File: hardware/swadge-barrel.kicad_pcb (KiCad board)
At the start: 2 copper layers, 70.4 x 89.6 mm, 45 parts, among them J1 USB_B_Micro, Q1 Q_NPN_BEC, SW4 SW_SPDT, U1 ESP-13-WROOM-02D, U2 DISP_OLED_UG-2864HSWEG01, U3 BUS_PCIexpress, U4 QMA6981, U5 AP1117-33

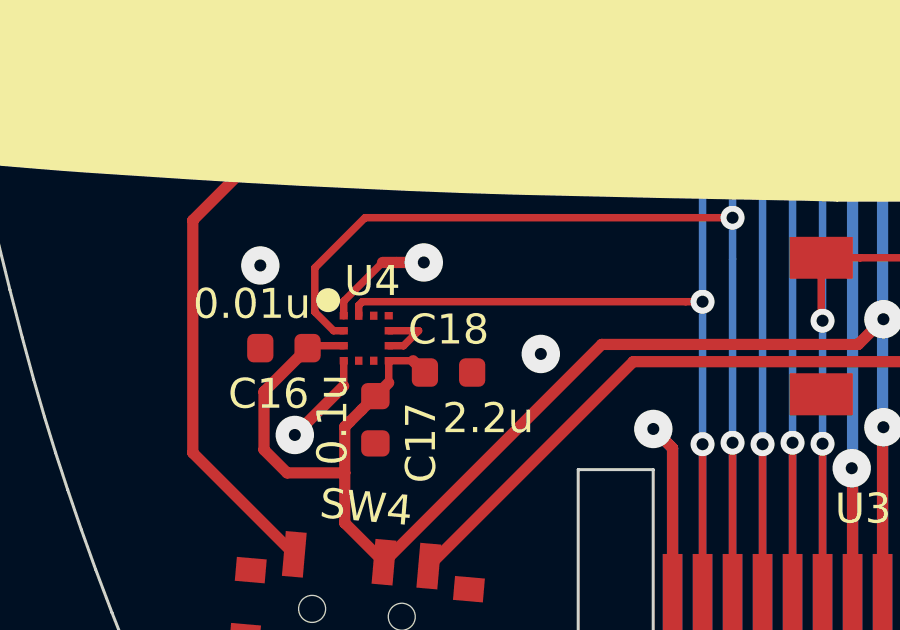
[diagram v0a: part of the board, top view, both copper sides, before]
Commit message: Updated ESP model
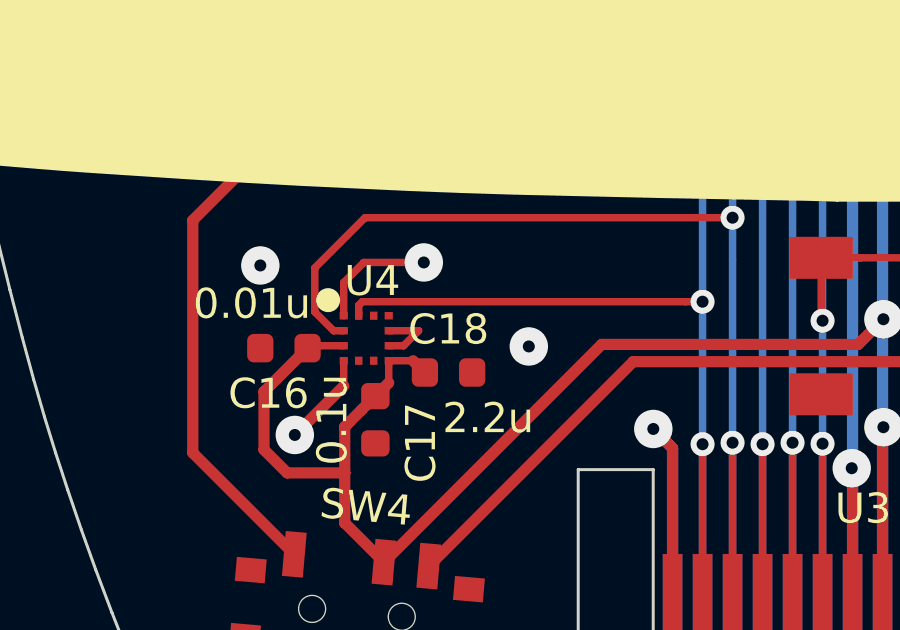
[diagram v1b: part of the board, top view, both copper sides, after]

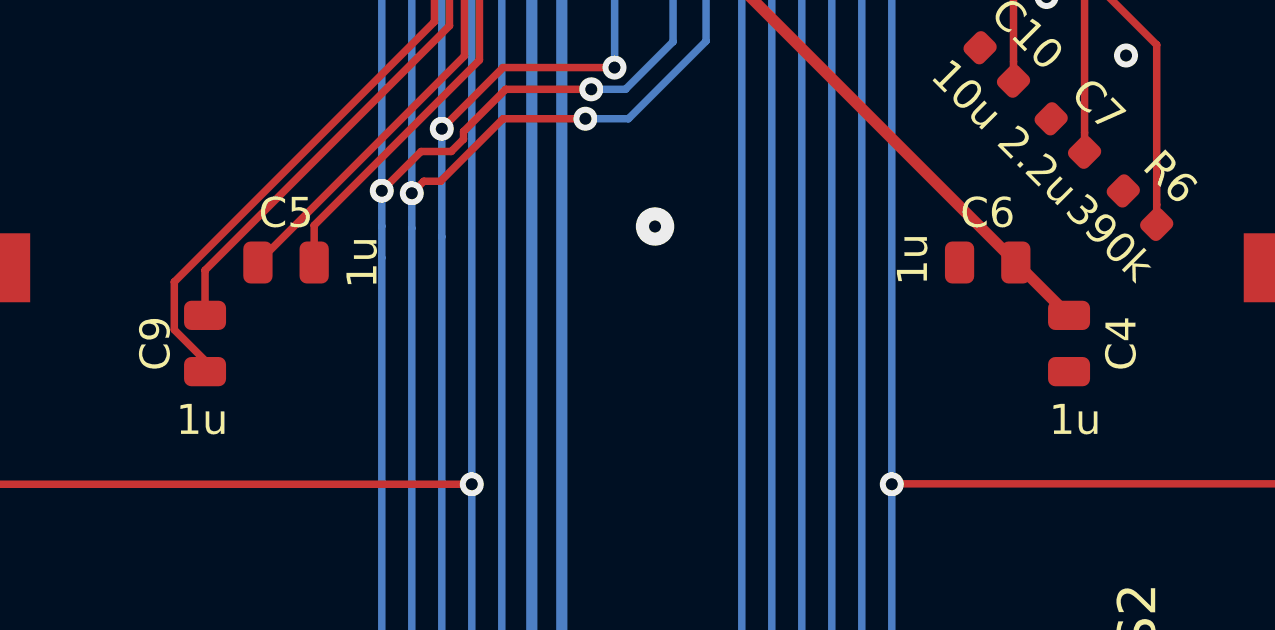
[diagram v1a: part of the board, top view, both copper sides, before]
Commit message: Added 0ohm support resistors
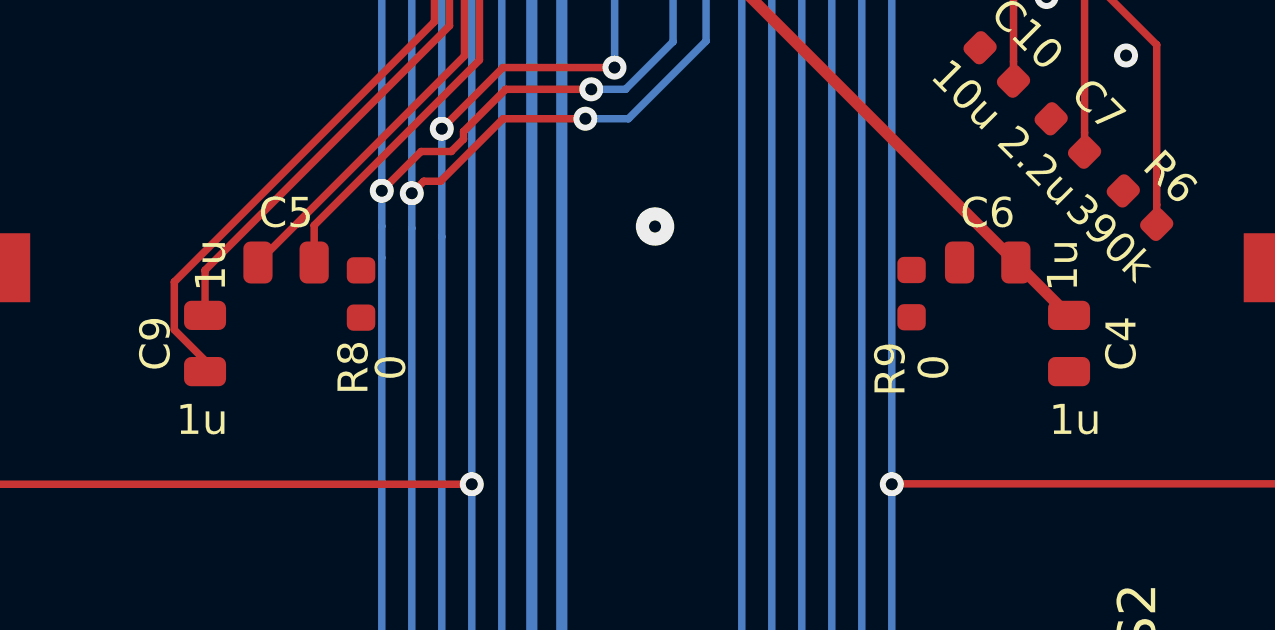
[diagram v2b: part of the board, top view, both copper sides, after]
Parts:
- added R8: 0, Swadge_Parts:R_0603_1608Metric, F.Cu at (136.3, 94.8)
- added R9: 0, Swadge_Parts:R_0603_1608Metric, F.Cu at (154.7, 94.8)
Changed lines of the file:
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@@
     (tracks 493)
     (zones 0)
-    (modules 45)
+    (modules 47)
     (nets 41)
   )
@@
     (uvia_drill 0.1)
   )
+  (module Swadge_Parts:R_0603_1608Metric (layer F.Cu)
+    (at 154.65 94.8375 90)
+    (descr "Resistor SMD 0603 (1608 Metric), square (rectangular) end terminal, IPC_7351 nominal, (Body size source: http://www.tortai-tech.com/upload/download/2011102023233369053.pdf), generated with kicad-footprint-generator")
+    (tags resistor)
+    (attr smd)
+    (fp_text reference R9 (at -2.5125 -0.7 90) (layer F.SilkS)
+      (effects (font (size 1 1) (thickness 0.15)))
+    )
+    (fp_text value 0 (at -2.4625 0.75 90) (layer F.SilkS)
+      (effects (font (size 1 1) (thickness 0.15)))
+    )
+    (fp_line (start -0.8 0.4) (end -0.8 -0.4) (layer F.Fab) (width 0.1))
+    (fp_line (start -0.8 -0.4) (end 0.8 -0.4) (layer F.Fab) (width 0.1))
+    (fp_line (start 0.8 -0.4) (end 0.8 0.4) (layer F.Fab) (width 0.1))
+    (fp_line (start 0.8 0.4) (end -0.8 0.4) (layer F.Fab) (width 0.1))
+    (fp_line (start -0.162779 -0.51) (end 0.162779 -0.51) (layer F.Fab) (width 0.12))
+    (fp_line (start -0.162779 0.51) (end 0.162779 0.51) (layer F.Fab) (width 0.12))
+    (fp_line (start -1.48 0.73) (end -1.48 -0.73) (layer F.CrtYd) (width 0.05))
+    (fp_line (start -1.48 -0.73) (end 1.48 -0.73) (layer F.CrtYd) (width 0.05))
+    (fp_line (start 1.48 -0.73) (end 1.48 0.73) (layer F.CrtYd) (width 0.05))
+    (fp_line (start 1.48 0.73) (end -1.48 0.73) (layer F.CrtYd) (width 0.05))
+    (fp_text user %R (at 0 0 90) (layer F.Fab)
+      (effects (font (size 0.4 0.4) (thickness 0.06)))
+    )
+    (pad 1 smd roundrect (at -0.7875 0 90) (size 0.875 0.95) (layers F.Cu F.Paste F.Mask) (roundrect_rratio 0.25)
+      (net 1 GND))
+    (pad 2 smd roundrect (at 0.7875 0 90) (size 0.875 0.95) (layers F.Cu F.Paste F.Mask) (roundrect_rratio 0.25)
+      (net 1 GND))
+    (model ${KIPRJMOD}/kicad-libs/package3d/R_0603_1608Metric.wrl
+      (at (xyz 0 0 0))
+      (scale (xyz 1 1 1))
+      (rotate (xyz 0 0 0))
+    )
+  )
+  (module Swadge_Parts:R_0603_1608Metric (layer F.Cu)
+    (at 136.3 94.85 90)
+    (descr "Resistor SMD 0603 (1608 Metric), square (rectangular) end terminal, IPC_7351 nominal, (Body size source: http://www.tortai-tech.com/upload/download/2011102023233369053.pdf), generated with kicad-footprint-generator")
+    (tags resistor)
+    (attr smd)
+    (fp_text reference R8 (at -2.45 -0.25 90) (layer F.SilkS)
+      (effects (font (size 1 1) (thickness 0.15)))
+    )
+    (fp_text value 0 (at -2.45 1 90) (layer F.SilkS)
+      (effects (font (size 1 1) (thickness 0.15)))
+    )
+    (fp_line (start -0.8 0.4) (end -0.8 -0.4) (layer F.Fab) (width 0.1))
+    (fp_line (start -0.8 -0.4) (end 0.8 -0.4) (layer F.Fab) (width 0.1))
+    (fp_line (start 0.8 -0.4) (end 0.8 0.4) (layer F.Fab) (width 0.1))
+    (fp_line (start 0.8 0.4) (end -0.8 0.4) (layer F.Fab) (width 0.1))
+    (fp_line (start -0.162779 -0.51) (end 0.162779 -0.51) (layer F.Fab) (width 0.12))
+    (fp_line (start -0.162779 0.51) (end 0.162779 0.51) (layer F.Fab) (width 0.12))
+    (fp_line (start -1.48 0.73) (end -1.48 -0.73) (layer F.CrtYd) (width 0.05))
+    (fp_line (start -1.48 -0.73) (end 1.48 -0.73) (layer F.CrtYd) (width 0.05))
+    (fp_line (start 1.48 -0.73) (end 1.48 0.73) (layer F.CrtYd) (width 0.05))
+    (fp_line (start 1.48 0.73) (end -1.48 0.73) (layer F.CrtYd) (width 0.05))
+    (fp_text user %R (at 0 0 90) (layer F.Fab)
+      (effects (font (size 0.4 0.4) (thickness 0.06)))
+    )
+    (pad 1 smd roundrect (at -0.7875 0 90) (size 0.875 0.95) (layers F.Cu F.Paste F.Mask) (roundrect_rratio 0.25)
+      (net 1 GND))
+    (pad 2 smd roundrect (at 0.7875 0 90) (size 0.875 0.95) (layers F.Cu F.Paste F.Mask) (roundrect_rratio 0.25)
+      (net 1 GND))
+    (model ${KIPRJMOD}/kicad-libs/package3d/R_0603_1608Metric.wrl
+      (at (xyz 0 0 0))
+      (scale (xyz 1 1 1))
+      (rotate (xyz 0 0 0))
+    )
+  )
   (module Swadge_Parts:ESP-13-WROOM-02 (layer F.Cu)
     (at 148.509589 60.463179 357)
@@
       (effects (font (size 1 1) (thickness 0.15)))
     )
-    (fp_text value 1u (at -2.4879 -0.1 90) (layer F.SilkS)
+    (fp_text value 1u (at 2.5121 0.1 90) (layer F.SilkS)
       (effects (font (size 1 1) (thickness 0.15)))
     )
@@
       (effects (font (size 1 1) (thickness 0.15)))
     )
-    (fp_text value 1u (at 2.55 0 90) (layer F.SilkS)
-      (effects (font (size 1 1) (thickness 0.15)))
-    )
+    (fp_text value 1u (at -2.5 0.1 90) (layer F.SilkS)
+      (effects (font (size 1 1) (thickness 0.15)))
+    )

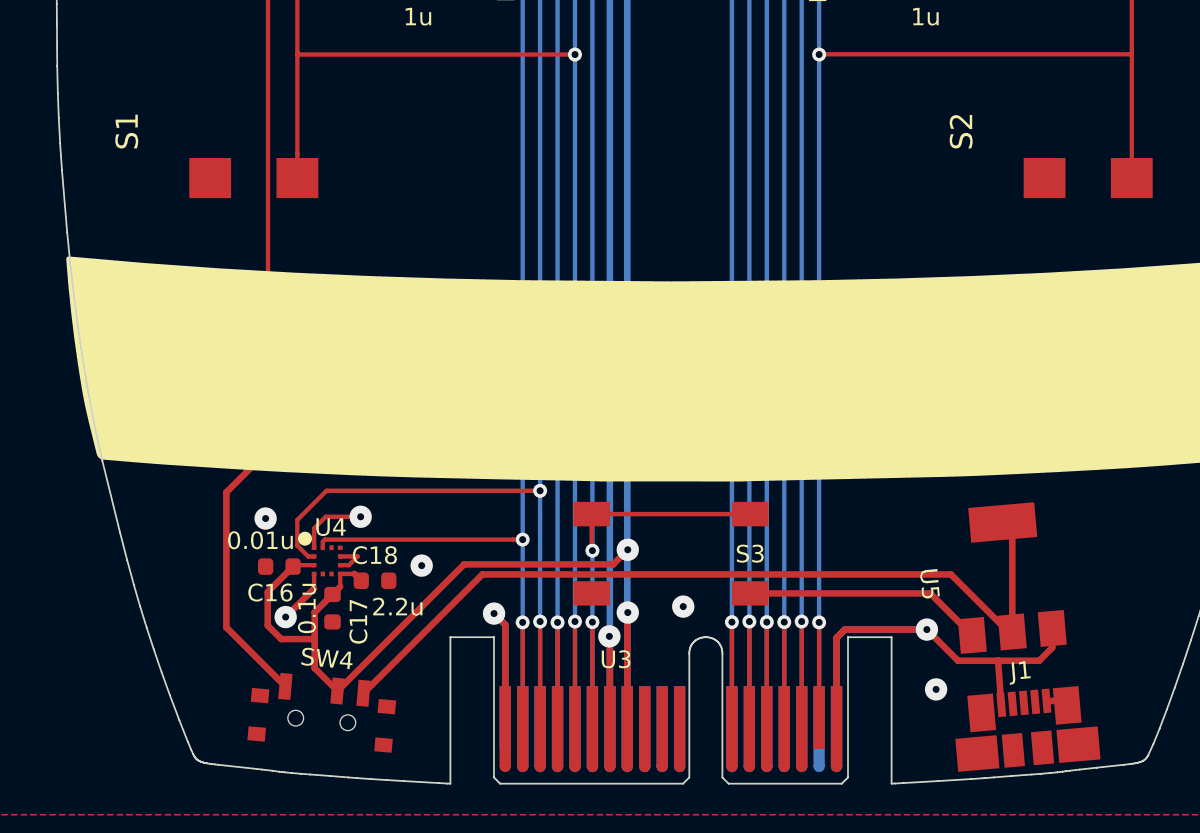
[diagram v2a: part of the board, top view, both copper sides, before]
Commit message: #21 added LED OUT to PCIe connector
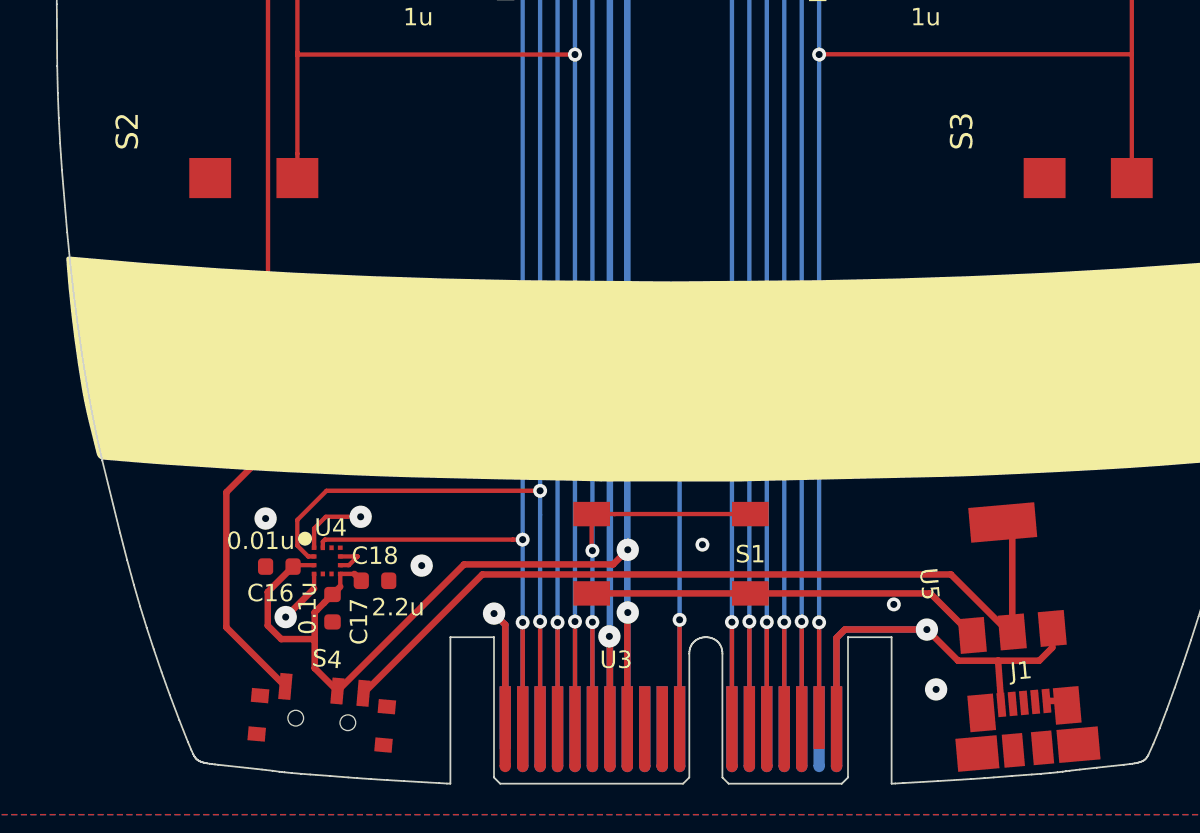
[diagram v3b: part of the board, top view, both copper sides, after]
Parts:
- renumbered S3 to S1, S1 to S2, S2 to S3, SW4 to S4
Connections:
- net SW5 renamed BZR
- D6 pad 2: (no net) -> LED_OUT
- S1 pad 1: SW3 -> SW1
- S1 pad 2: SW3 -> SW1
- S3 pad 1: SW4 -> SW3
- S3 pad 2: SW4 -> SW3
- U1 pad 10: SW4 -> SW3
- U1 pad 4: SW3 -> SW1
- U3 pad A11: Net-(U3-PadA11) -> LED_OUT
- U3 pad A17: SW4 -> SW3
- U3 pad A6: SW3 -> SW1
- U3 pad B11: Net-(U3-PadB11) -> LED_OUT
- U3 pad B17: SW4 -> SW3
- U3 pad B6: SW3 -> SW1
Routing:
- net SW4: track 110.5 -> 0.00 mm, vias 3 -> 0
- net SW1: track 0.00 -> 100.1 mm, vias 0 -> 3
- net LED_OUT: track 0.00 -> 53.7 mm, vias 0 -> 2
- net SW3: track 100.1 -> 110.5 mm
- net GND: track 69.8 -> 78.9 mm, vias 13 -> 14

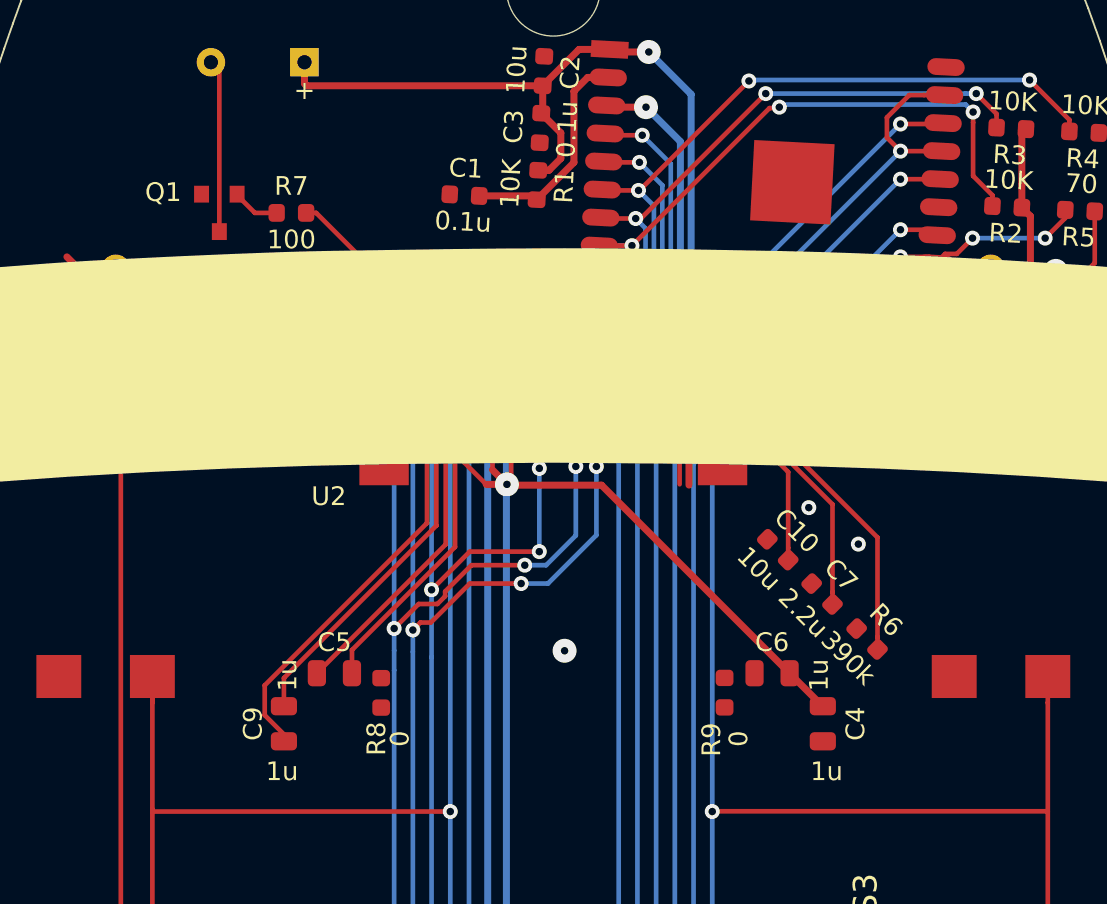
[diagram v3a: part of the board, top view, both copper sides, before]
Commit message: Switched to elecrow FPC part. moved around things. added art, version
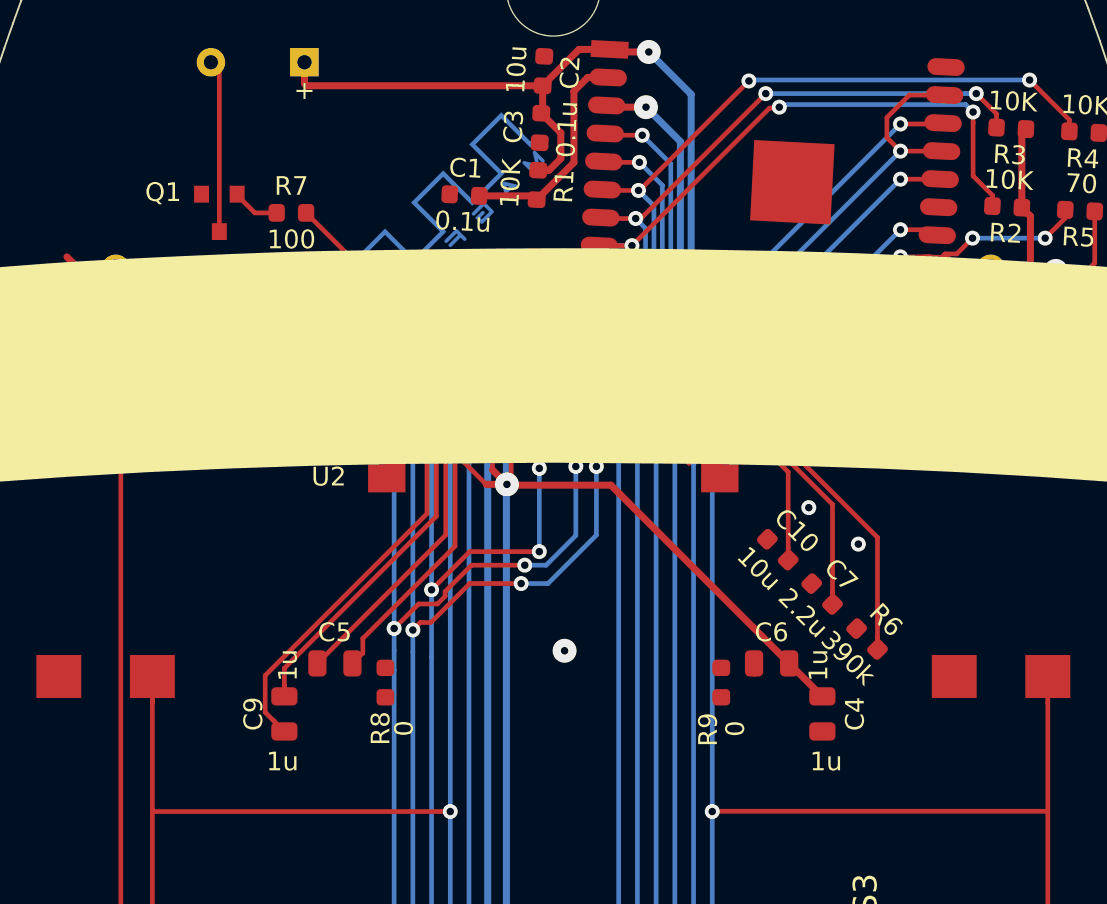
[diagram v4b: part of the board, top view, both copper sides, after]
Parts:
- added svg2mod: G***, Swadge_Parts:MAGFEST_logo_centered_final, B.Cu at (139.3, 69.5)
- U2: footprint Swadge_Parts:oled-flat -> Swadge_Parts:oled-flat_copy
- moved U2 1.04 mm to (145.5, 93.8)
- moved D2 0.66 mm to (145.5, 76.5)
- moved R8 0.59 mm to (136.5, 94.3)
- moved R9 0.57 mm to (154.5, 94.3)
- moved C4 0.53 mm to (159.9, 96.0)
- moved C9 0.53 mm to (131.1, 96.0)
- moved C6 0.53 mm to (157.2, 93.3)
- moved C5 0.53 mm to (133.8, 93.3)
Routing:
- net GND: track 78.9 -> 89.2 mm, vias 14 -> 13
- net +3V3: track 305.8 -> 308.5 mm
- net SDA: track 143.8 -> 145.9 mm
- net Net-(D1-Pad2): track 18.4 -> 19.9 mm, vias 0 -> 2
- net SCL: track 138.9 -> 139.9 mm
- net _RES: track 125.6 -> 126.7 mm
- net Net-(BT1-Pad1): track 49.7 -> 50.4 mm
- net Net-(C9-Pad1): track 20.1 -> 20.6 mm
- net Net-(C5-Pad1): track 15.3 -> 15.8 mm
- net Net-(C5-Pad2): track 14.8 -> 15.3 mm
- net Net-(C9-Pad2): track 17.6 -> 18.1 mm
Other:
- board text added: "Barrel 1.0.0"
